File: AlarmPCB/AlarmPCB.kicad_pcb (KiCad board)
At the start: 2 copper layers, 99.9 x 74 mm, 17 parts

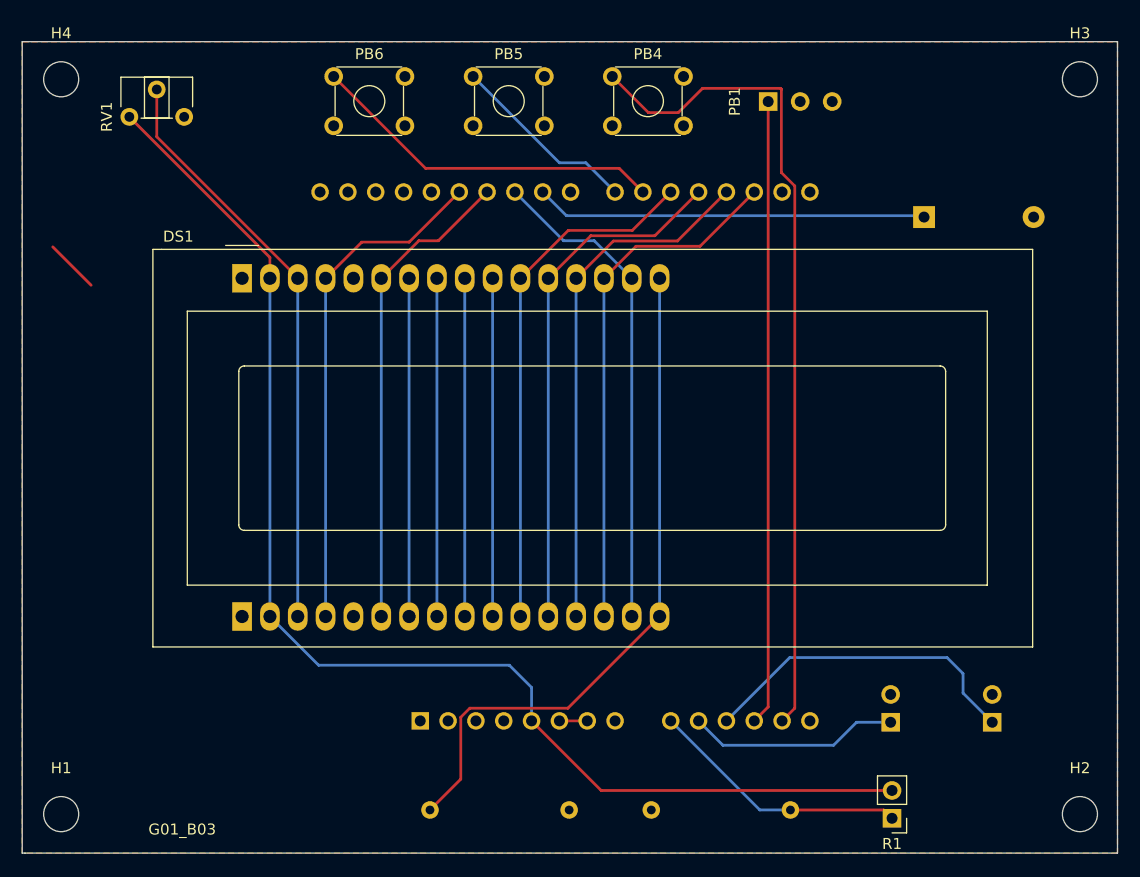
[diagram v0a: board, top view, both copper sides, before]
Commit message: Updated Footprints
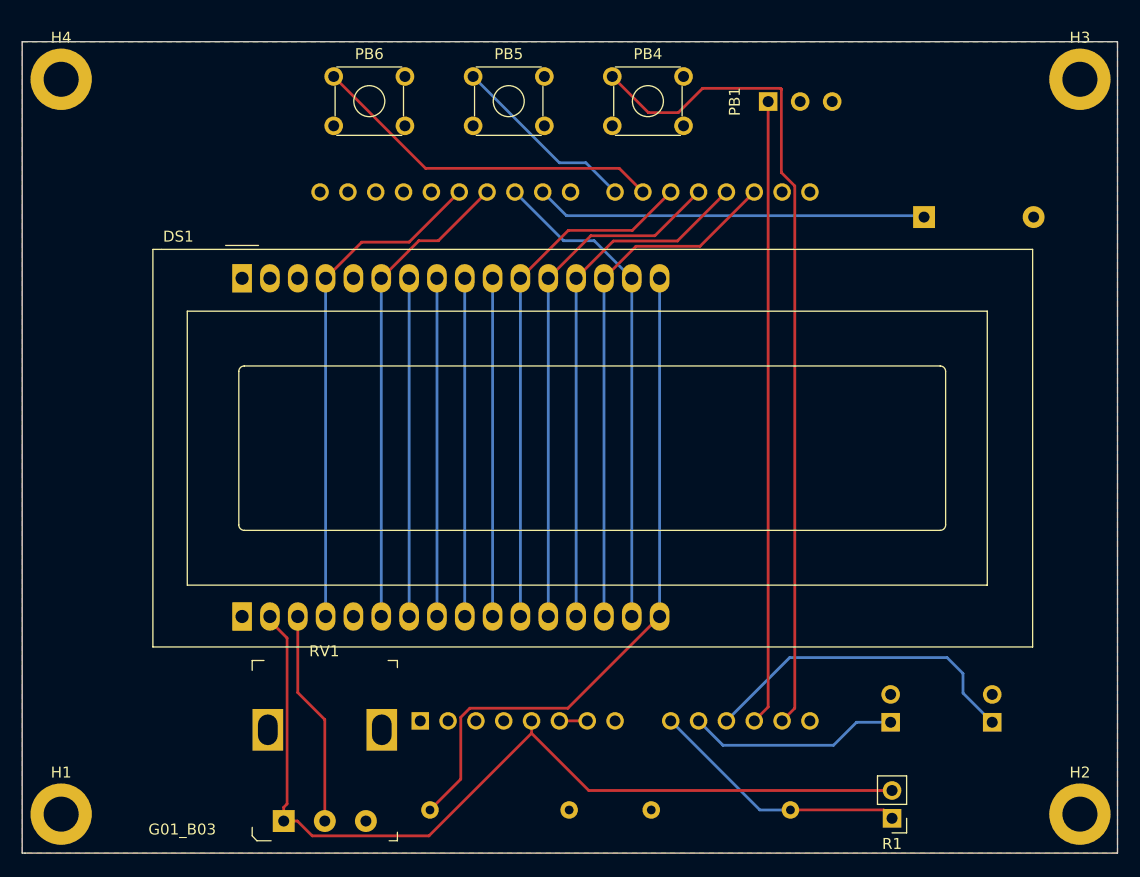
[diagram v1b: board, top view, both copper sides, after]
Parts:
- H1, H2, H3, H4: footprint MountingHole:MountingHole_3.2mm_M3 -> MountingHole:MountingHole_3.2mm_M3_DIN965_Pad
- RV1: footprint Potentiometer_THT:Potentiometer_ACP_CA6-H2,5_Horizontal -> digikey-footprints:Potentiometer_P120PK-Y25BR10K
- moved RV1 65.8 mm to (96.0, 167.0), turned to 0 degrees
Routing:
- net Net-(DS1-Pad3): track 53.4 -> 19.7 mm
- net +5V: track 116.0 -> 82.7 mm
- net GND: track 7.49 -> 2.54 mm
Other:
- board text added: "G01B03"

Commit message: Revert "Updated Footprints"
This reverts commit dd3b0c72e674ffb159cfd3c8d42ceca2805da80f.
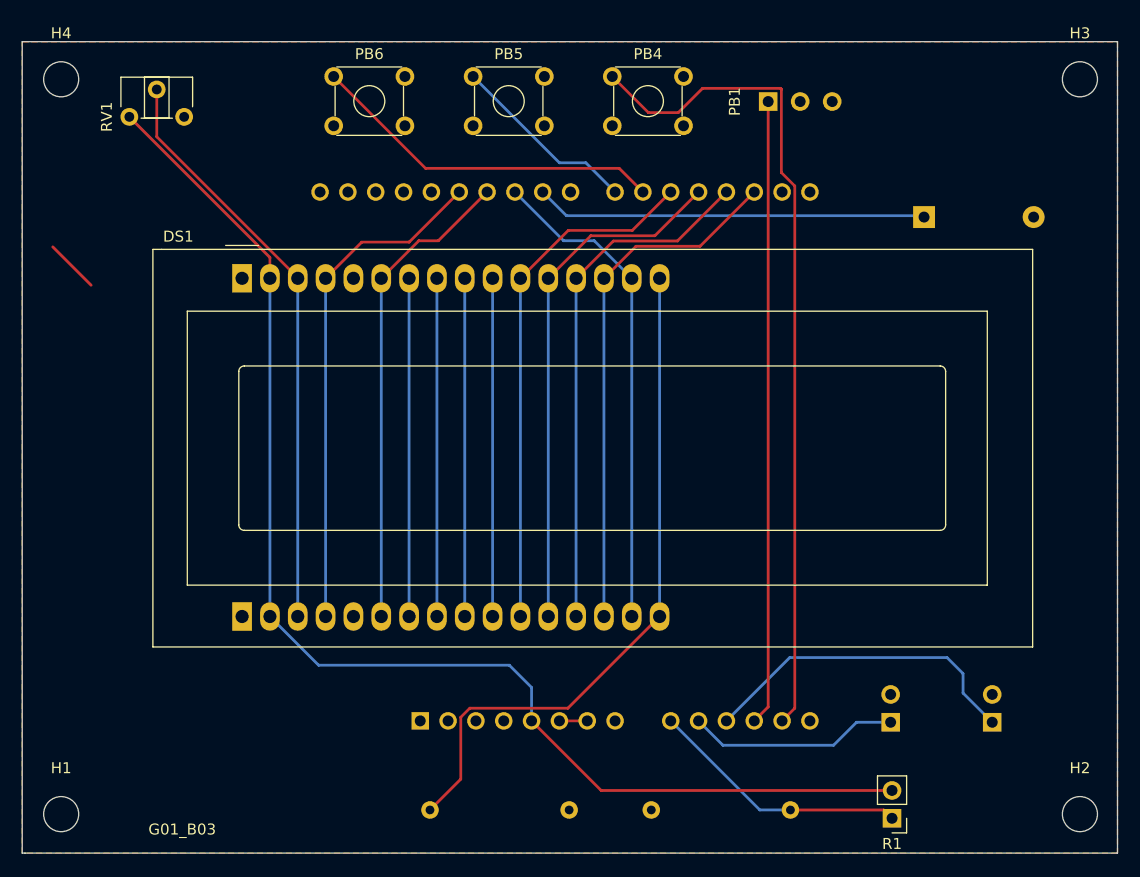
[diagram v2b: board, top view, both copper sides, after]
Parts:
- H1, H2, H3, H4: footprint MountingHole:MountingHole_3.2mm_M3_DIN965_Pad -> MountingHole:MountingHole_3.2mm_M3
- RV1: footprint digikey-footprints:Potentiometer_P120PK-Y25BR10K -> Potentiometer_THT:Potentiometer_ACP_CA6-H2,5_Horizontal
- moved RV1 65.8 mm to (81.9, 102.7), turned to 90 degrees
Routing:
- net Net-(DS1-Pad3): track 19.7 -> 53.4 mm
- net +5V: track 82.7 -> 116.0 mm
- net GND: track 2.54 -> 7.49 mm
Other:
- board text removed: "G01B03"
